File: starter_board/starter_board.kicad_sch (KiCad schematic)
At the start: 42 parts, among them J1 Conn_01x10, J2 Conn_01x10, J3 ICSP, J4 USB_B_Micro, U1 ATmega32U4-A, Y1 16MHz

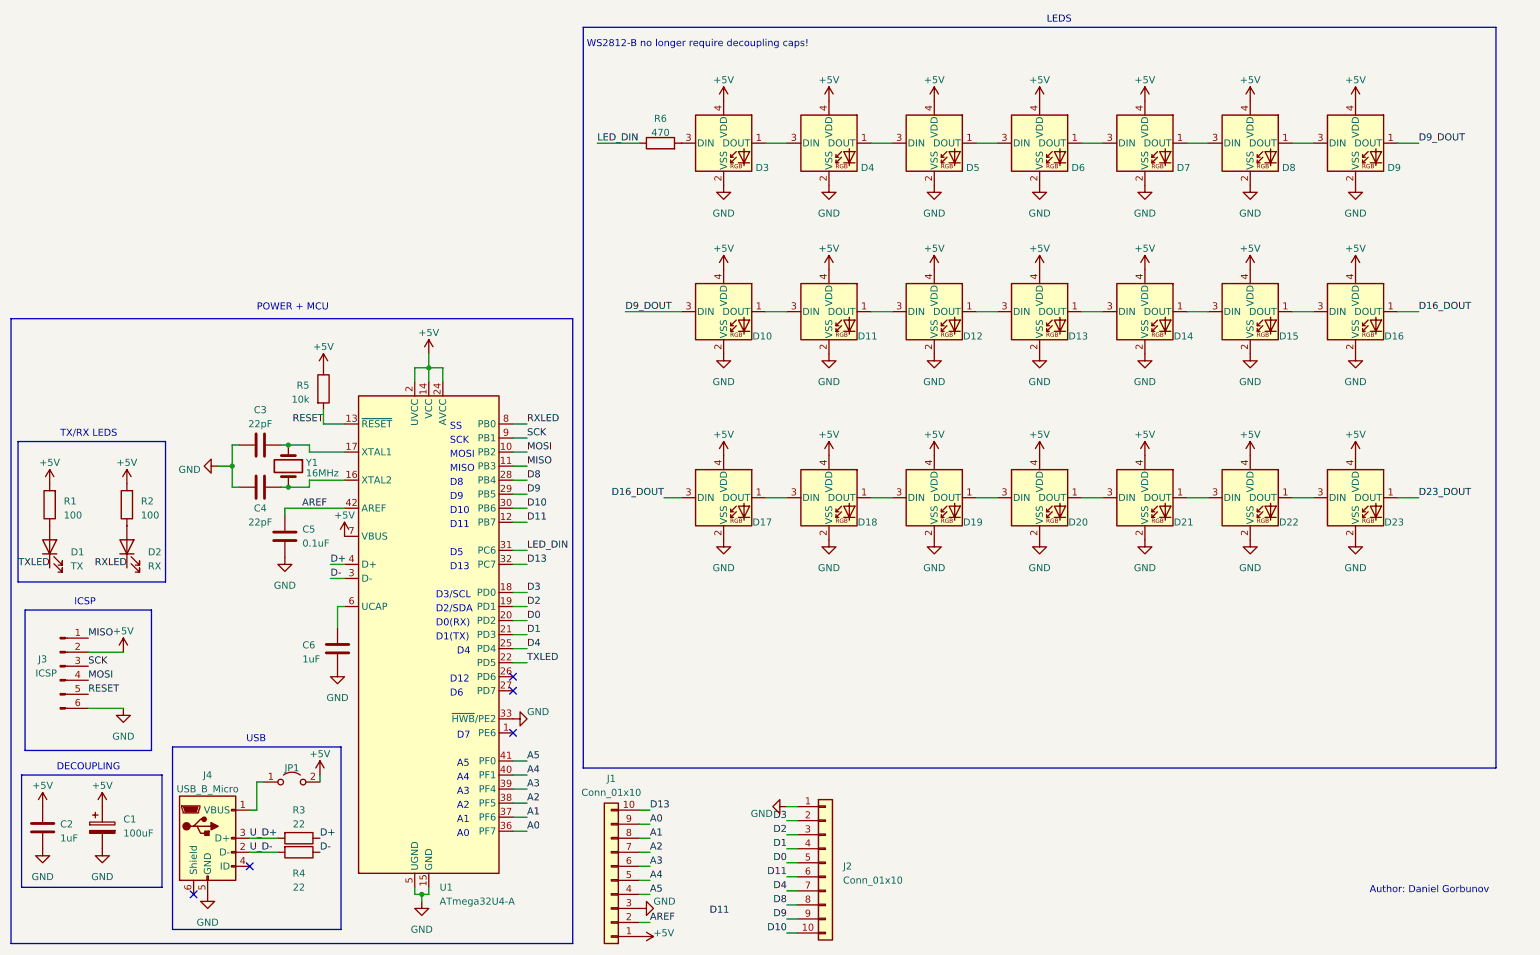
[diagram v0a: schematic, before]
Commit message: Update starter board for KiCad 9.0.7
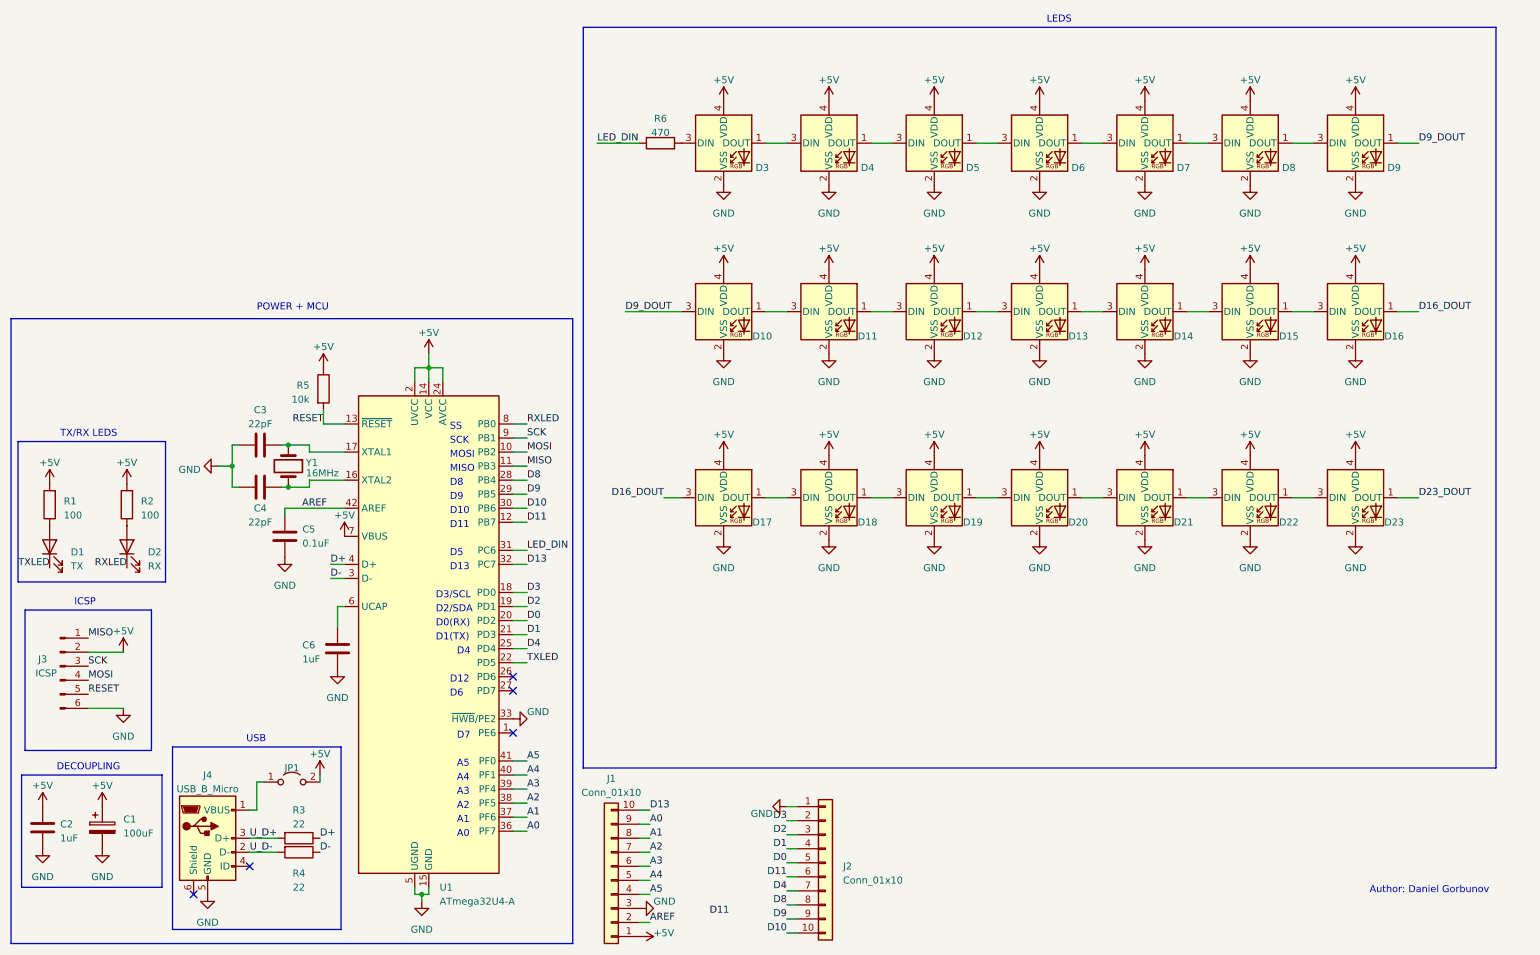
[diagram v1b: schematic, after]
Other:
- note removed: "WS2812-B no longer require decoupling caps!"
